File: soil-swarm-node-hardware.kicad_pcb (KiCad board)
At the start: 2 copper layers, 100 x 22.5 mm, 40 parts, among them J1 USB_B_Micro, J2 BATT_CONN, J3 Conn_01x07, Q1 Q_NMOS_GSD, Q2 DMP3099L-13, Q3 DMP3099L-13, U1 RFD77101, U2 MCP73811T-420I-OT, U3 TLV74130, U4 DS18B20U, U5 SST26VF016B

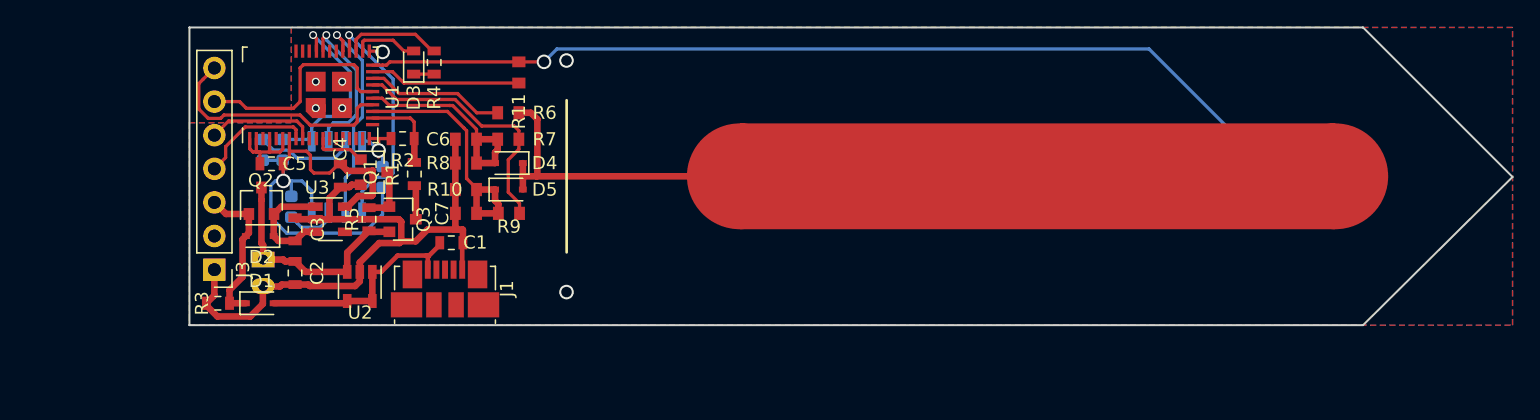
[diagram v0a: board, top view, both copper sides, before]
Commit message: create new version based on nRF52840
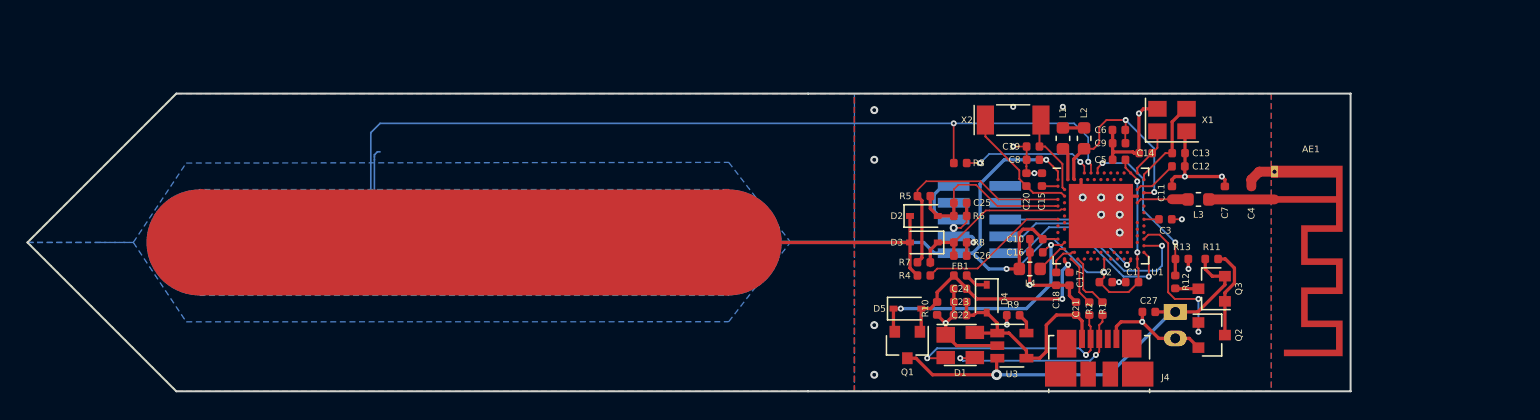
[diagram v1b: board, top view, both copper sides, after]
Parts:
- removed the C*** at (146.3, 92.3)
- removed the G*** at (122.5, 92.3)
- removed J2: BATT_CONN, Connector_JST:JST_PH_S2B-PH-K_1x02_P2.00mm_Horizontal
- removed R14: 100k, Resistor_SMD:R_0603_1608Metric
- removed U4: DS18B20U, Package_SO:MSOP-8_3x3mm_P0.65mm
- removed U5: SST26VF016B, Package_SO:SOIC-8_3.9x4.9mm_P1.27mm
- added AE1: Antenna, RF_Antenna:Texas_SWRA117D_2.4GHz_Right, F.Cu at (164.2, 94.0)
- added C***: SENSE, soil-swarm-node-hardware:c_layout_2, B.Cu at (103.0, 97.2)
- added C***: SENSE, soil-swarm-node-hardware:c_layout_1, F.Cu at (103.0, 97.2)
- added C10: 4,7µF, Capacitor_SMD:C_0402_1005Metric, F.Cu at (146.2, 97.0)
- added C11: 1pF, Capacitor_SMD:C_0402_1005Metric, F.Cu at (156.5, 93.5)
- added C12: 100pF, Capacitor_SMD:C_0402_1005Metric, F.Cu at (157.0, 91.5)
- added C13: 12pF, Capacitor_SMD:C_0402_1005Metric, F.Cu at (157.0, 90.5)
- added C14: 12pF, Capacitor_SMD:C_0402_1005Metric, F.Cu at (154.5, 90.5)
- added C15: 100nF, Capacitor_SMD:C_0402_1005Metric, F.Cu at (146.7, 92.5)
- added C16: 4,7µF, Capacitor_SMD:C_0402_1005Metric, F.Cu at (146.2, 98.0)
- added C17: 4,7µF, Capacitor_SMD:C_0402_1005Metric, F.Cu at (148.8, 100.0)
- added C18: 4,7µF, Capacitor_SMD:C_0402_1005Metric, F.Cu at (147.8, 100.0)
- added C19: 12pF, Capacitor_SMD:C_0402_1005Metric, F.Cu at (146.0, 90.0)
- added C20: 12pF, Capacitor_SMD:C_0402_1005Metric, F.Cu at (145.5, 92.5)
- added C21: 10µF, Capacitor_SMD:C_0402_1005Metric, F.Cu at (149.2, 102.2)
- added C22: 100nF, Capacitor_SMD:C_0402_1005Metric, F.Cu at (140.5, 102.8)
- added C23: 10nF, Capacitor_SMD:C_0402_1005Metric, F.Cu at (140.5, 101.8)
- added C24: 100nF, Capacitor_SMD:C_0402_1005Metric, F.Cu at (140.5, 100.8)
- added C25: 1n, Capacitor_SMD:C_0402_1005Metric, F.Cu at (140.5, 94.2)
- added C26: 1n, Capacitor_SMD:C_0402_1005Metric, F.Cu at (140.5, 98.2)
- added C27: 4.7u, Capacitor_SMD:C_0402_1005Metric, F.Cu at (154.8, 102.5)
- added C9: 47nF, Capacitor_SMD:C_0402_1005Metric, F.Cu at (152.5, 89.8)
- added FB1: 120R/0,55A, Inductor_SMD:L_0402_1005Metric, F.Cu at (140.5, 99.8)
- added G***: LOGO, misc:TU_Logo_Framed, B.Cu at (122.0, 97.2)
- added J4: USB_B_Micro, Connector_USB:USB_Micro-B_Molex_47346-0001, F.Cu at (151.0, 106.0)
- added L1: 15nH, Inductor_SMD:L_0603_1608Metric, F.Cu at (148.3, 89.4)
- added L2: 10µH, Inductor_SMD:L_0603_1608Metric, F.Cu at (149.9, 89.4)
- added L3: 3,9nH, Inductor_SMD:L_0603_1608Metric, F.Cu at (158.5, 94.0)
- added L4: 10µH, Inductor_SMD:L_0603_1608Metric, F.Cu at (145.8, 99.2)
- added X1: 32MHz, Crystal:Crystal_SMD_3225-4Pin_3.2x2.5mm, F.Cu at (156.5, 88.0)
- added X2: 32,768kHz, Crystal:Crystal_SMD_MicroCrystal_CC4V-T1A-2Pin_5.0x1.9mm, F.Cu at (144.5, 88.0)
- C1, C2: value 4.7u -> 100nF; footprint Capacitor_SMD:C_0603_1608Metric -> Capacitor_SMD:C_0402_1005Metric
- C3: value 1u -> 820pF; footprint Capacitor_SMD:C_0603_1608Metric -> Capacitor_SMD:C_0402_1005Metric
- C4: value 1u -> N.C.; footprint Capacitor_SMD:C_0603_1608Metric -> Capacitor_SMD:C_0402_1005Metric
- C5: value 1u -> 100nF; footprint Capacitor_SMD:C_0603_1608Metric -> Capacitor_SMD:C_0402_1005Metric
- C6: value 1n -> 1µF; footprint Capacitor_SMD:C_0603_1608Metric -> Capacitor_SMD:C_0402_1005Metric
- C7: value 1n -> 1pF; footprint Capacitor_SMD:C_0603_1608Metric -> Capacitor_SMD:C_0402_1005Metric
- C8: value 0.1u -> 1µF; footprint Capacitor_SMD:C_0603_1608Metric -> Capacitor_SMD:C_0402_1005Metric; moved to F.Cu
- D1: value BAT20J -> PRTR5V0U2X; footprint Diode_SMD:D_SOD-323 -> Package_TO_SOT_SMD:SOT-143
- D2: value BAT20J -> BAT54
- D3: value LED -> BAT54; footprint LED_SMD:LED_0603_1608Metric -> Diode_SMD:D_SOD-323
- D4, D5: value BAT54 -> BAT20J
- J1: value USB_B_Micro -> Conn_ARM_JTAG_SWD_10; footprint Connector_USB:USB_Micro-B_Molex_47346-0001 -> Connector_PinHeader_1.27mm:PinHeader_2x05_P1.27mm_Vertical_SMD; moved to B.Cu
- J3: value Conn_01x07 -> BATT_CONN; footprint Connector_PinHeader_2.54mm:PinHeader_1x07_P2.54mm_Vertical -> Connector_JST:JST_PH_S2B-PH-K_1x02_P2.00mm_Horizontal; moved to B.Cu
- Q1: value Q_NMOS_GSD -> DMP3099L-13
- Q2: value DMP3099L-13 -> Q_NMOS_GSD
- R1: value 3.1k -> 0; footprint Resistor_SMD:R_0603_1608Metric -> Resistor_SMD:R_0402_1005Metric
- R10: value 1M -> 10k; footprint Resistor_SMD:R_0603_1608Metric -> Resistor_SMD:R_0402_1005Metric
- R11: value 4.7k -> 10k; footprint Resistor_SMD:R_0603_1608Metric -> Resistor_SMD:R_0402_1005Metric
- R12: value 100k -> 3.1k; footprint Resistor_SMD:R_0603_1608Metric -> Resistor_SMD:R_0402_1005Metric; moved to F.Cu
- R13: value 100k -> 8.2k; footprint Resistor_SMD:R_0603_1608Metric -> Resistor_SMD:R_0402_1005Metric; moved to F.Cu
- R2: value 8.2k -> 0; footprint Resistor_SMD:R_0603_1608Metric -> Resistor_SMD:R_0402_1005Metric
- R3: value 10k -> 4.7k; footprint Resistor_SMD:R_0603_1608Metric -> Resistor_SMD:R_0402_1005Metric
- R4: value 47 -> 330; footprint Resistor_SMD:R_0603_1608Metric -> Resistor_SMD:R_0402_1005Metric
- R5: value 10k -> 1M; footprint Resistor_SMD:R_0603_1608Metric -> Resistor_SMD:R_0402_1005Metric
- R6: value 330 -> 1M; footprint Resistor_SMD:R_0603_1608Metric -> Resistor_SMD:R_0402_1005Metric
- R7, R8: footprint Resistor_SMD:R_0603_1608Metric -> Resistor_SMD:R_0402_1005Metric
- R9: value 1M -> R; footprint Resistor_SMD:R_0603_1608Metric -> Resistor_SMD:R_0402_1005Metric
- U1: value RFD77101 -> nRF52840; footprint RF_Module:RFDigital_RFD77101 -> Package_DFN_QFN:Nordic_AQFN-73-1EP_7x7mm_P0.5mm
- U2: value MCP73811T-420I-OT -> DS18B20U; footprint Package_TO_SOT_SMD:SOT-23-5 -> Package_SO:MSOP-8_3x3mm_P0.65mm; moved to B.Cu
- U3: value TLV74130 -> MCP73812T-420I-OT
- moved J3 72.7 mm to (156.8, 102.5), turned to 270 degrees
- moved Q2 72.5 mm to (159.5, 104.2), turned to 0 degrees
- moved R13 69.9 mm to (157.2, 98.5), turned to 0 degrees
- moved C4 68.9 mm to (162.5, 93.5), turned to 90 degrees
- moved R12 67.1 mm to (156.8, 100.2), turned to 90 degrees
- moved C3 65.8 mm to (156.0, 95.5), turned to 0 degrees
- moved C5 64.1 mm to (152.5, 91.0)
- moved Q3 61.4 mm to (159.5, 100.8), turned to 180 degrees
- moved C2 61.3 mm to (151.5, 100.2), turned to 0 degrees
- moved U1 60.5 mm to (151.1, 95.2), turned to 0 degrees
- moved C7 57.4 mm to (160.5, 93.5), turned to 90 degrees
- moved R3 57.1 mm to (140.5, 91.2)
- moved R11 54.2 mm to (159.5, 98.5), turned to 0 degrees
- moved R2 53.5 mm to (150.2, 102.2), turned to 90 degrees
- moved D1 53.0 mm to (140.5, 105.0)
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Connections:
- C1 pad 1: Net-(C1-Pad1) -> VCC
- C2 pad 1: +BATT -> VCC
- C3 pad 1: Net-(C3-Pad1) -> /DEC5
- C4 pad 1: VDD -> Net-(AE1-Pad1)
- C5 pad 1: VDD -> VCC
- C6 pad 1: /SENSE_LOW -> /DEC4
- C7 pad 1: /SENSE_HIGH -> Net-(AE1-Pad1)
- C8 pad 1: VDD -> VCC
- D1 pad 1: VBUS -> GND
- D1 pad 2: Net-(C1-Pad1) -> Net-(D1-Pad2)
- D2 pad 1: Net-(C3-Pad1) -> /SENSE_TRACK
- D2 pad 2: VBUS -> /SENSE_LOW
- D3 pad 1: Net-(D3-Pad1) -> /SENSE_HIGH
- D3 pad 2: /LED_1_I -> /SENSE_TRACK
- D4 pad 1: /SENSE_TRACK -> Net-(D4-Pad1)
- D4 pad 2: /SENSE_LOW -> /soil-swarm-node-hardware-components/V_USB
- D5 pad 1: /SENSE_HIGH -> LINE
- D5 pad 2: /SENSE_TRACK -> VBUS
- J1 pad 1: Net-(C1-Pad1) -> VCC
- J1 pad 2: (no net) -> /SWDIO
- J1 pad 3: (no net) -> GND
- J1 pad 4: (no net) -> /SWDCLK
- J1 pad 6: Net-(J1-Pad6) -> /SWO
- J3 pad 1: GND -> +BATT
- J3 pad 2: (no net) -> GND
- Q1 pad 1: /BATT_V_EN -> VBUS
- Q1 pad 2: GND -> LINE
- Q1 pad 3: Net-(Q1-Pad3) -> +BATT
- Q2 pad 1: VBUS -> /BATT_V_EN
- Q2 pad 2: Net-(C3-Pad1) -> GND
- Q2 pad 3: +BATT -> Net-(Q2-Pad3)
- Q3 pad 1: Net-(Q1-Pad3) -> Net-(Q2-Pad3)
- R1 pad 1: Net-(Q3-Pad3) -> /D+
- R1 pad 2: /BATT_V -> Net-(D1-Pad3)
- R10 pad 1: /SENSE_HIGH -> GND
- R10 pad 2: GND -> VBUS
- R11 pad 1: /TEMP_DATA -> +BATT
- R11 pad 2: /TEMP_EN -> Net-(Q2-Pad3)
- R12 pad 1: VDD -> Net-(Q3-Pad3)
- R12 pad 2: Net-(R12-Pad2) -> /BATT_V
- R13 pad 1: VDD -> /BATT_V
- R13 pad 2: Net-(R13-Pad2) -> GND
- R2 pad 1: /BATT_V -> Net-(D1-Pad2)
- R2 pad 2: GND -> /D-
- R3 pad 1: VBUS -> /TEMP_EN
- R3 pad 2: GND -> /TEMP_DATA
- R4 pad 1: Net-(D3-Pad1) -> /SENSE_TRACK
- R4 pad 2: /LED_1_O -> /EXCITATION
- R5 pad 1: +BATT -> /SENSE_EN
- R5 pad 2: Net-(Q1-Pad3) -> /SENSE_LOW
- R6 pad 1: /SENSE_TRACK -> /SENSE_LOW
- R6 pad 2: /EXCITATION -> GND
- R7 pad 2: /SENSE_LOW -> /SENSE_HIGH
- R8 pad 1: /SENSE_LOW -> /SENSE_HIGH
- R9 pad 1: /SENSE_EN -> Net-(R9-Pad1)
- R9 pad 2: /SENSE_HIGH -> GND
- U2 pad 1: Net-(C1-Pad1) -> /TEMP_DATA
- U2 pad 2: GND -> (no net)
- U2 pad 3: +BATT -> (no net)
- U2 pad 4: Net-(C1-Pad1) -> GND
- U2 pad 5: Net-(C1-Pad1) -> (no net)
- U3 pad 1: Net-(C3-Pad1) -> /soil-swarm-node-hardware-components/V_USB
- U3 pad 3: Net-(C3-Pad1) -> +BATT
- U3 pad 4: (no net) -> /soil-swarm-node-hardware-components/V_USB
- U3 pad 5: VDD -> Net-(R9-Pad1)
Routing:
- net VCC: track 0.00 -> 67.9 mm, vias 0 -> 5
- net VDD: track 39.6 -> 0.00 mm, vias 1 -> 0
- net /SENSE_TRACK: track 41.2 -> 19.4 mm
- net LINE: track 0.00 -> 19.4 mm, vias 0 -> 2
- net /GPIO1: track 18.7 -> 0.00 mm
- net /soil-swarm-node-hardware-components/V_USB: track 0.00 -> 17.8 mm
- net /SPI_MOSI: track 17.6 -> 0.00 mm, vias 1 -> 0
- net Net-(D1-Pad2): track 0.00 -> 17.1 mm, vias 0 -> 2
- net Net-(C1-Pad1): track 17.0 -> 0.00 mm
- net /GPIO0: track 16.8 -> 0.00 mm
- net GND: track 65.5 -> 82.2 mm, vias 8 -> 26
- net /DEC4: track 0.00 -> 16.3 mm, vias 0 -> 2
- net /SPI_SCK: track 16.2 -> 0.00 mm, vias 1 -> 0
- net /SPI_SS: track 15.5 -> 0.00 mm, vias 1 -> 0
- net +BATT: track 18.0 -> 33.2 mm, vias 0 -> 1
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- added copper zone on B.Cu, net VCC
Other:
- outline, holes or cut-outs redrawn
- net class Default: clearance 0.2 -> 0.145; via_dia 0.6 -> 0.8
- rule pad_to_mask_clearance: 0.2 -> 0.051
- rule trace_clearance: 0.2 -> 0.145
- rule trace_min: 0.2 -> 0.0889
- rule via_min_drill: 0.3 -> 0.2
- rule via_min_size: 0.4 -> 0.45
- board text added: "soil-swarm-node-hardware-v2.0.0"

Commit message: finalizing 2.0.0
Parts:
- C1, C15, C2, C22, C24, C5: value 100nF -> 100n
- C10, C16, C17, C18: value 4,7µF -> 4.7u
- C11, C7: value 1pF -> 1p
- C12: value 100pF -> 100p
- C13, C14, C19, C20: value 12pF -> 12p
- C21: value 10µF -> 10u
- C23: value 10nF -> 10n
- C3: value 820pF -> 820p
- C6, C8: value 1µF -> 1u
- C9: value 47nF -> 47n
- L1: value 15nH -> 15n
- L2, L4: value 10µH -> 10u
- L3: value 3,9nH -> 3.9n
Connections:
- AE1 pad 2: GND -> (no net)
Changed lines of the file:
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@@
       (effects (font (size 0.5 0.5) (thickness 0.05)))
     )
-    (fp_text value 4,7µF (at 0 1.17 270) (layer F.Fab)
+    (fp_text value 4.7u (at 0 1.17 270) (layer F.Fab)
       (effects (font (size 0.8 0.5) (thickness 0.05)))
     )
@@
       (effects (font (size 0.5 0.5) (thickness 0.05)))
     )
-    (fp_text value 10nF (at 0 1.17 180) (layer F.Fab)
+    (fp_text value 10n (at 0 1.17 180) (layer F.Fab)
       (effects (font (size 0.8 0.5) (thickness 0.05)))
     )
@@
       (effects (font (size 0.5 0.5) (thickness 0.05)))
     )
-    (fp_text value 100nF (at 0 1.17 180) (layer F.Fab)
+    (fp_text value 100n (at 0 1.17 180) (layer F.Fab)
       (effects (font (size 0.8 0.5) (thickness 0.05)))
     )
@@
       (effects (font (size 0.5 0.5) (thickness 0.05)))
     )
-    (fp_text value 100pF (at 0 1.17) (layer F.Fab)
+    (fp_text value 100p (at 0 1.17) (layer F.Fab)
       (effects (font (size 0.8 0.5) (thickness 0.05)))
     )
@@
       (effects (font (size 0.5 0.5) (thickness 0.05)))
     )
-    (fp_text value 12pF (at 0 1.17 270) (layer F.Fab)
+    (fp_text value 12p (at 0 1.17 270) (layer F.Fab)
       (effects (font (size 0.8 0.5) (thickness 0.05)))
     )
@@
       (effects (font (size 0.5 0.5) (thickness 0.05)))
     )
-    (fp_text value 820pF (at 0 1.17) (layer F.Fab)
+    (fp_text value 820p (at 0 1.17) (layer F.Fab)
       (effects (font (size 0.8 0.5) (thickness 0.05)))
     )
@@
       (effects (font (size 0.5 0.5) (thickness 0.05)))
     )
-    (fp_text value 1µF (at 0 1.17 180) (layer F.Fab)
+    (fp_text value 1u (at 0 1.17 180) (layer F.Fab)
       (effects (font (size 0.8 0.5) (thickness 0.05)))
     )
@@
       (effects (font (size 0.5 0.5) (thickness 0.05)))
     )
-    (fp_text value 1pF (at 0 1.17 90) (layer F.Fab)
+    (fp_text value 1p (at 0 1.17 90) (layer F.Fab)
       (effects (font (size 0.8 0.5) (thickness 0.05)))
     )
@@
       (effects (font (size 0.5 0.5) (thickness 0.05)))
     )
-    (fp_text value 47nF (at 0 1.17 180) (layer F.Fab)
+    (fp_text value 47n (at 0 1.17 180) (layer F.Fab)
       (effects (font (size 0.8 0.5) (thickness 0.05)))
     )
@@
       (effects (font (size 0.5 0.5) (thickness 0.05)))
     )
-    (fp_text value 4,7µF (at 0 1.17 180) (layer F.Fab)
+    (fp_text value 4.7u (at 0 1.17 180) (layer F.Fab)
       (effects (font (size 0.8 0.5) (thickness 0.05)))
     )
@@
       (effects (font (size 0.5 0.5) (thickness 0.05)))
     )
-    (fp_text value 1pF (at 0 1.17 90) (layer F.Fab)
+    (fp_text value 1p (at 0 1.17 90) (layer F.Fab)
       (effects (font (size 0.8 0.5) (thickness 0.05)))
     )
@@
       (effects (font (size 0.5 0.5) (thickness 0.05)))
     )
-    (fp_text value 12pF (at 0 1.17 180) (layer F.Fab)
+    (fp_text value 12p (at 0 1.17 180) (layer F.Fab)
       (effects (font (size 0.8 0.5) (thickness 0.05)))
     )
@@
       (effects (font (size 0.5 0.5) (thickness 0.05)))
     )
-    (fp_text value 12pF (at 0 1.17) (layer F.Fab)
+    (fp_text value 12p (at 0 1.17) (layer F.Fab)
       (effects (font (size 0.8 0.5) (thickness 0.05)))
     )
@@
       (effects (font (size 0.5 0.5) (thickness 0.05)))
     )
-    (fp_text value 100nF (at 0 1.17 90) (layer F.Fab)
+    (fp_text value 100n (at 0 1.17 90) (layer F.Fab)
       (effects (font (size 0.8 0.5) (thickness 0.05)))
     )
@@
       (effects (font (size 0.5 0.5) (thickness 0.05)))
     )
-    (fp_text value 4,7µF (at 0 1.17 180) (layer F.Fab)
+    (fp_text value 4.7u (at 0 1.17 180) (layer F.Fab)
       (effects (font (size 0.8 0.5) (thickness 0.05)))
     )
@@
       (effects (font (size 0.5 0.5) (thickness 0.05)))
     )
-    (fp_text value 4,7µF (at 0 1.17 270) (layer F.Fab)
+    (fp_text value 4.7u (at 0 1.17 270) (layer F.Fab)
       (effects (font (size 0.8 0.5) (thickness 0.05)))
     )
@@
       (effects (font (size 0.5 0.5) (thickness 0.05)))
     )
-    (fp_text value 12pF (at 0 1.17) (layer F.Fab)
+    (fp_text value 12p (at 0 1.17) (layer F.Fab)
       (effects (font (size 0.8 0.5) (thickness 0.05)))
     )
@@
       (effects (font (size 0.5 0.5) (thickness 0.05)))
     )
-    (fp_text value 15nH (at 0 1.43 90) (layer F.Fab)
+    (fp_text value 15n (at 0 1.43 90) (layer F.Fab)
       (effects (font (size 0.8 0.5) (thickness 0.05)))
     )
@@
       (effects (font (size 0.5 0.5) (thickness 0.05)))
     )
-    (fp_text value 10µH (at 0 1.43 270) (layer F.Fab)
+    (fp_text value 10u (at 0 1.43 270) (layer F.Fab)
       (effects (font (size 0.8 0.5) (thickness 0.05)))
     )
@@
       (effects (font (size 0.5 0.5) (thickness 0.05)))
     )
-    (fp_text value 3,9nH (at 0 1.43 180) (layer F.Fab)
+    (fp_text value 3.9n (at 0 1.43 180) (layer F.Fab)
       (effects (font (size 0.8 0.5) (thickness 0.05)))
     )
@@
       (effects (font (size 0.5 0.5) (thickness 0.05)))
     )
-    (fp_text value 10µH (at 0 1.43) (layer F.Fab)
+    (fp_text value 10u (at 0 1.43) (layer F.Fab)
       (effects (font (size 0.8 0.5) (thickness 0.05)))
     )
@@
       (effects (font (size 0.5 0.5) (thickness 0.05)))
     )
-    (fp_text value 10µF (at 0 1.17 90) (layer F.Fab)
+    (fp_text value 10u (at 0 1.17 90) (layer F.Fab)
       (effects (font (size 0.8 0.5) (thickness 0.05)))
     )
@@
       (effects (font (size 0.5 0.5) (thickness 0.05)))
     )
-    (fp_text value 100nF (at 0 1.17 180) (layer F.Fab)
+    (fp_text value 100n (at 0 1.17 180) (layer F.Fab)
       (effects (font (size 0.8 0.5) (thickness 0.05)))
     )
@@
       (effects (font (size 0.5 0.5) (thickness 0.05)))
     )
-    (fp_text value 100nF (at 0 1.17 180) (layer F.Fab)
+    (fp_text value 100n (at 0 1.17 180) (layer F.Fab)
       (effects (font (size 0.8 0.5) (thickness 0.05)))
     )
@@
       (effects (font (size 0.5 0.5) (thickness 0.05)))
     )
-    (fp_text value 100nF (at 0 1.17) (layer F.Fab)
+    (fp_text value 100n (at 0 1.17) (layer F.Fab)
       (effects (font (size 0.8 0.5) (thickness 0.05)))
     )
@@
       (effects (font (size 0.5 0.5) (thickness 0.05)))
     )
-    (fp_text value 100nF (at 0 1.17 180) (layer F.Fab)
+    (fp_text value 100n (at 0 1.17 180) (layer F.Fab)
       (effects (font (size 0.8 0.5) (thickness 0.05)))
     )
@@
       (effects (font (size 0.5 0.5) (thickness 0.05)))
     )
-    (fp_text value 1µF (at 0 1.17 180) (layer F.Fab)
+    (fp_text value 1u (at 0 1.17 180) (layer F.Fab)
       (effects (font (size 0.8 0.5) (thickness 0.05)))
     )
@@
     (fp_line (start -3.2 -5.6) (end 12.3 -5.6) (layer F.Fab) (width 0.15))
     (pad 2 thru_hole rect (at -2.1 0 270) (size 0.9 0.5) (drill 0.3) (layers *.Cu)
-      (net 9 GND) (zone_connect 2))
+      (zone_connect 2))
     (pad 1 connect rect (at 0 0 270) (size 0.5 0.5) (layers F.Cu)
       (net 37 "Net-(AE1-Pad1)"))

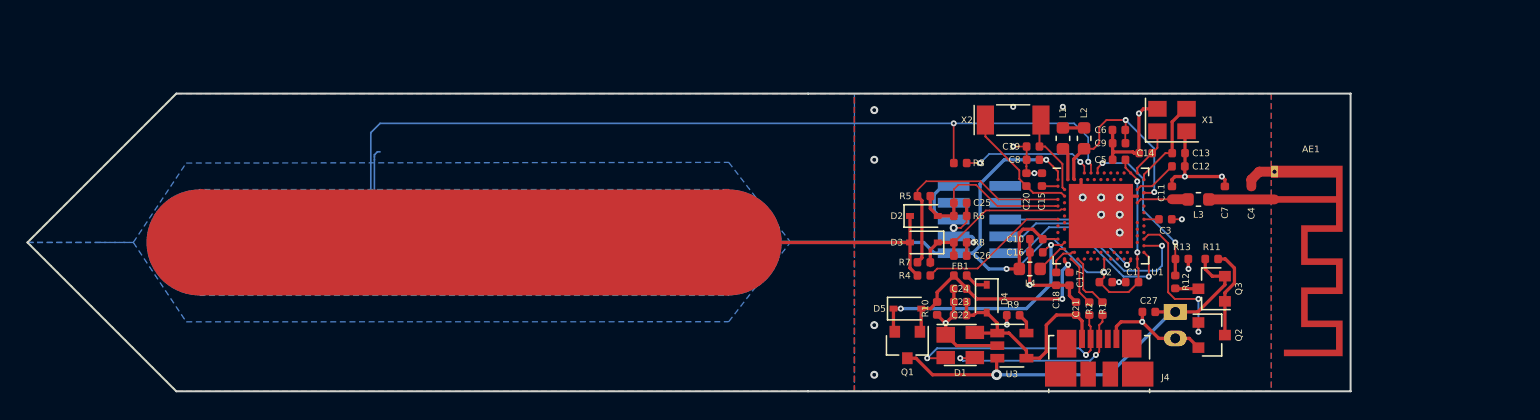
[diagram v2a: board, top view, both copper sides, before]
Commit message: update based on Nordic specification
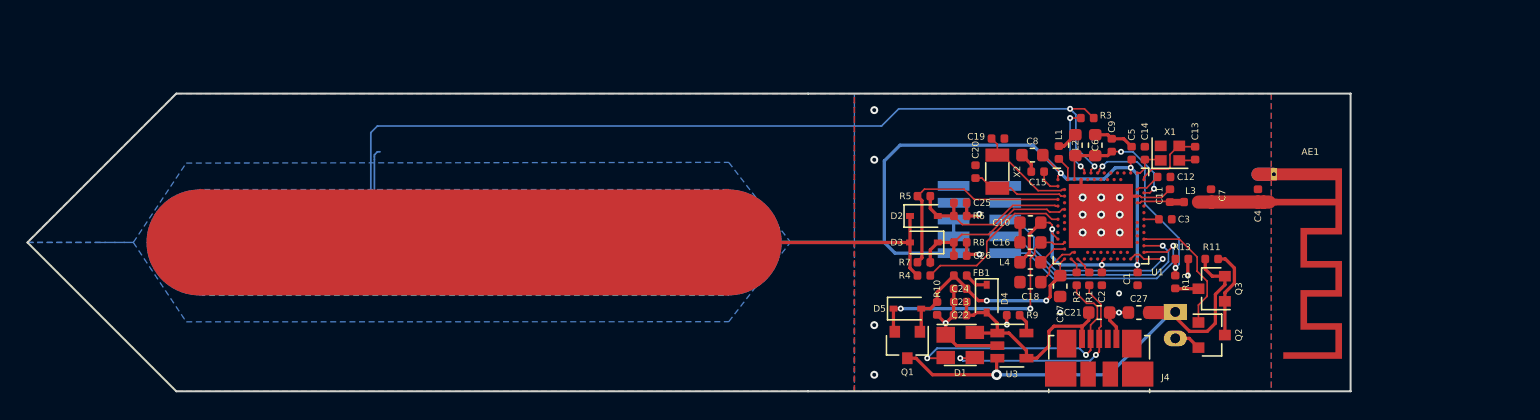
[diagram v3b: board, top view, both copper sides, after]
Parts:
- C10, C16, C17, C18, C21, C27, C6, C8: footprint Capacitor_SMD:C_0402_1005Metric -> Capacitor_SMD:C_0603_1608Metric
- L1, L3: footprint Inductor_SMD:L_0603_1608Metric -> Inductor_SMD:L_0402_1005Metric
- X1: footprint Crystal:Crystal_SMD_3225-4Pin_3.2x2.5mm -> Crystal:Crystal_SMD_2016-4Pin_2.0x1.6mm
- X2: footprint Crystal:Crystal_SMD_MicroCrystal_CC4V-T1A-2Pin_5.0x1.9mm -> Crystal:Crystal_SMD_3215-2Pin_3.2x1.5mm
- moved R3 10.2 mm to (150.1, 87.8), turned to 0 degrees
- moved X2 4.08 mm to (143.3, 91.9), turned to 270 degrees
- moved C20 3.90 mm to (141.7, 91.9)
- moved C19 2.72 mm to (143.3, 89.4), turned to 180 degrees
- moved X1 2.50 mm to (156.3, 90.5)
- moved R1 2.46 mm to (150.2, 100.0)
- moved R2 2.44 mm to (149.3, 100.0)
- moved C6 2.12 mm to (150.7, 89.9), turned to 90 degrees
- moved C18 1.97 mm to (145.8, 100.2), turned to 180 degrees
- moved C21 1.78 mm to (151.0, 102.5), turned to 0 degrees
- moved C12 1.35 mm to (155.9, 92.3)
- moved C10 1.33 mm to (145.8, 95.8)
- moved C13 1.25 mm to (158.2, 90.5), turned to 90 degrees
- moved L1 1.11 mm to (147.9, 90.5)
- moved C5 1.07 mm to (153.4, 90.5), turned to 90 degrees
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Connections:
- AE1 pad 2: (no net) -> GND
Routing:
- net GND: track 82.2 -> 51.5 mm, vias 26 -> 21
- net /SWO: track 11.2 -> 17.1 mm
- net VCC: track 67.9 -> 73.7 mm
- net /DEC4: track 16.3 -> 10.7 mm
- net /TEMP_EN: track 10.1 -> 5.41 mm
- net Net-(D1-Pad2): track 17.1 -> 20.5 mm
- net +BATT: track 33.2 -> 36.4 mm
- net /D+: track 4.32 -> 1.38 mm
- net /D-: track 3.83 -> 1.19 mm
- net Net-(D1-Pad3): track 14.9 -> 17.4 mm
- net /SWDIO: track 15.2 -> 17.7 mm
- net /XL2: track 9.47 -> 7.30 mm
- net /BATT_V_EN: track 11.6 -> 10.1 mm, vias 2 -> 0
- net /DEC3: track 3.34 -> 1.93 mm
- net /XC1: track 7.04 -> 5.63 mm
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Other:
- board text added: "soil-swarm-node-hardware-v2.0.1"
- board text removed: "soil-swarm-node-hardware-v2.0.0"

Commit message: C11 GND only via F23
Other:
- board text added: "soil-swarm-node-hardware-v2.0.2"
- board text removed: "soil-swarm-node-hardware-v2.0.1"
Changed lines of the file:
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@@
     )
   )
-  (gr_text soil-swarm-node-hardware-v2.0.1 (at 105.8 87.4 180) (layer B.SilkS)
+  (gr_text soil-swarm-node-hardware-v2.0.2 (at 105.8 87.4 180) (layer B.SilkS)
     (effects (font (size 1 1) (thickness 0.25)) (justify mirror))
   )
@@
       )
     )
+  )
+  (zone (net 0) (net_name "") (layer F.Cu) (hatch edge 0.508)
+    (connect_pads (clearance 0))
+    (min_thickness 0.254)
+    (keepout (tracks allowed) (vias allowed) (copperpour not_allowed))
+    (fill (arc_segments 16) (thermal_gap 0.508) (thermal_bridge_width 0.508))
+    (polygon
+      (pts
+        (xy 155.8 92.7) (xy 156.9 92.7) (xy 156.9 93.75) (xy 155.8 93.75)
+      )
+    )
